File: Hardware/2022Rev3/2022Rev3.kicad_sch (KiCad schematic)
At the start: 101 parts, among them J1 Conn_01x04, J4 Conn_01x09, J5 Conn_01x09, J6 Conn_01x03, Q1 Q_NMOS_DGS, Q2 Q_NMOS_DGS, Q3 Q_NMOS_DSG, SW1 SW_SPDT, U1 ACS758xCB-200B-PFF, U2 LT1910, U3 TRS12433, U4 TRS12450, U5 Teensy4.1_DEV-16771, U6 Opamp_Dual, U7 Opamp_Dual, U8 Opamp_Dual, U9 Opamp_Dual

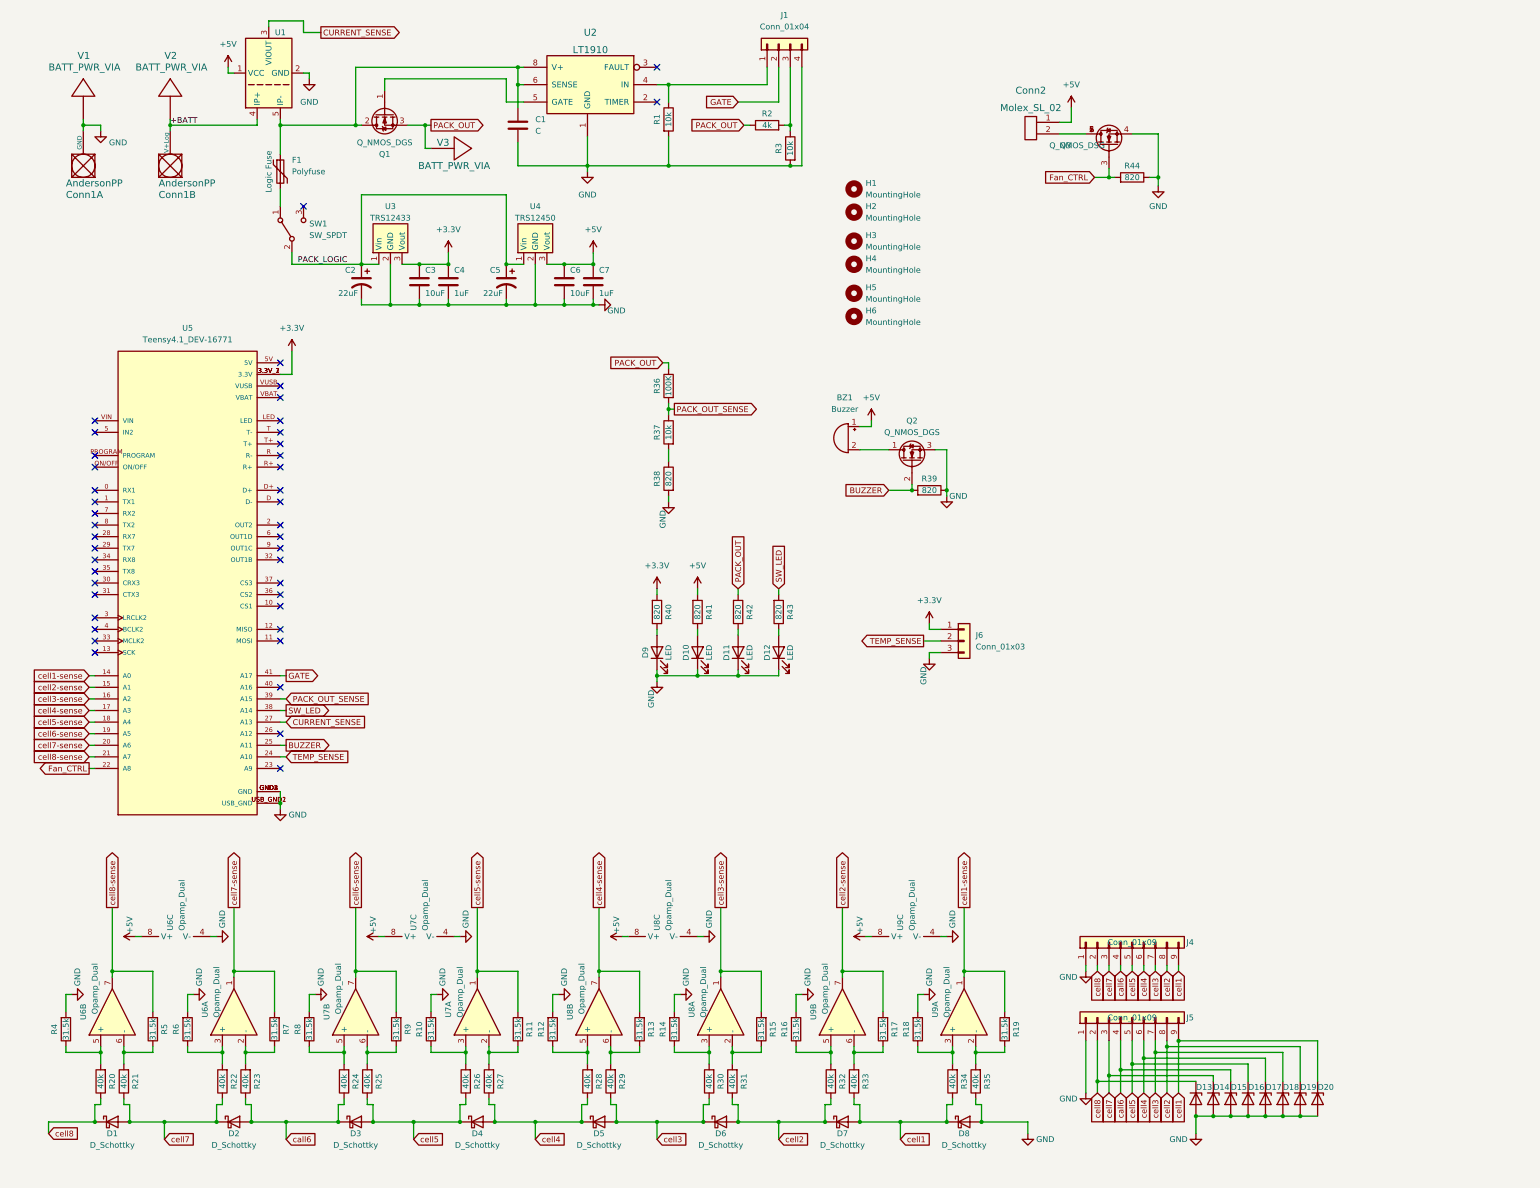
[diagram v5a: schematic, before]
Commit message: fixed led circuits
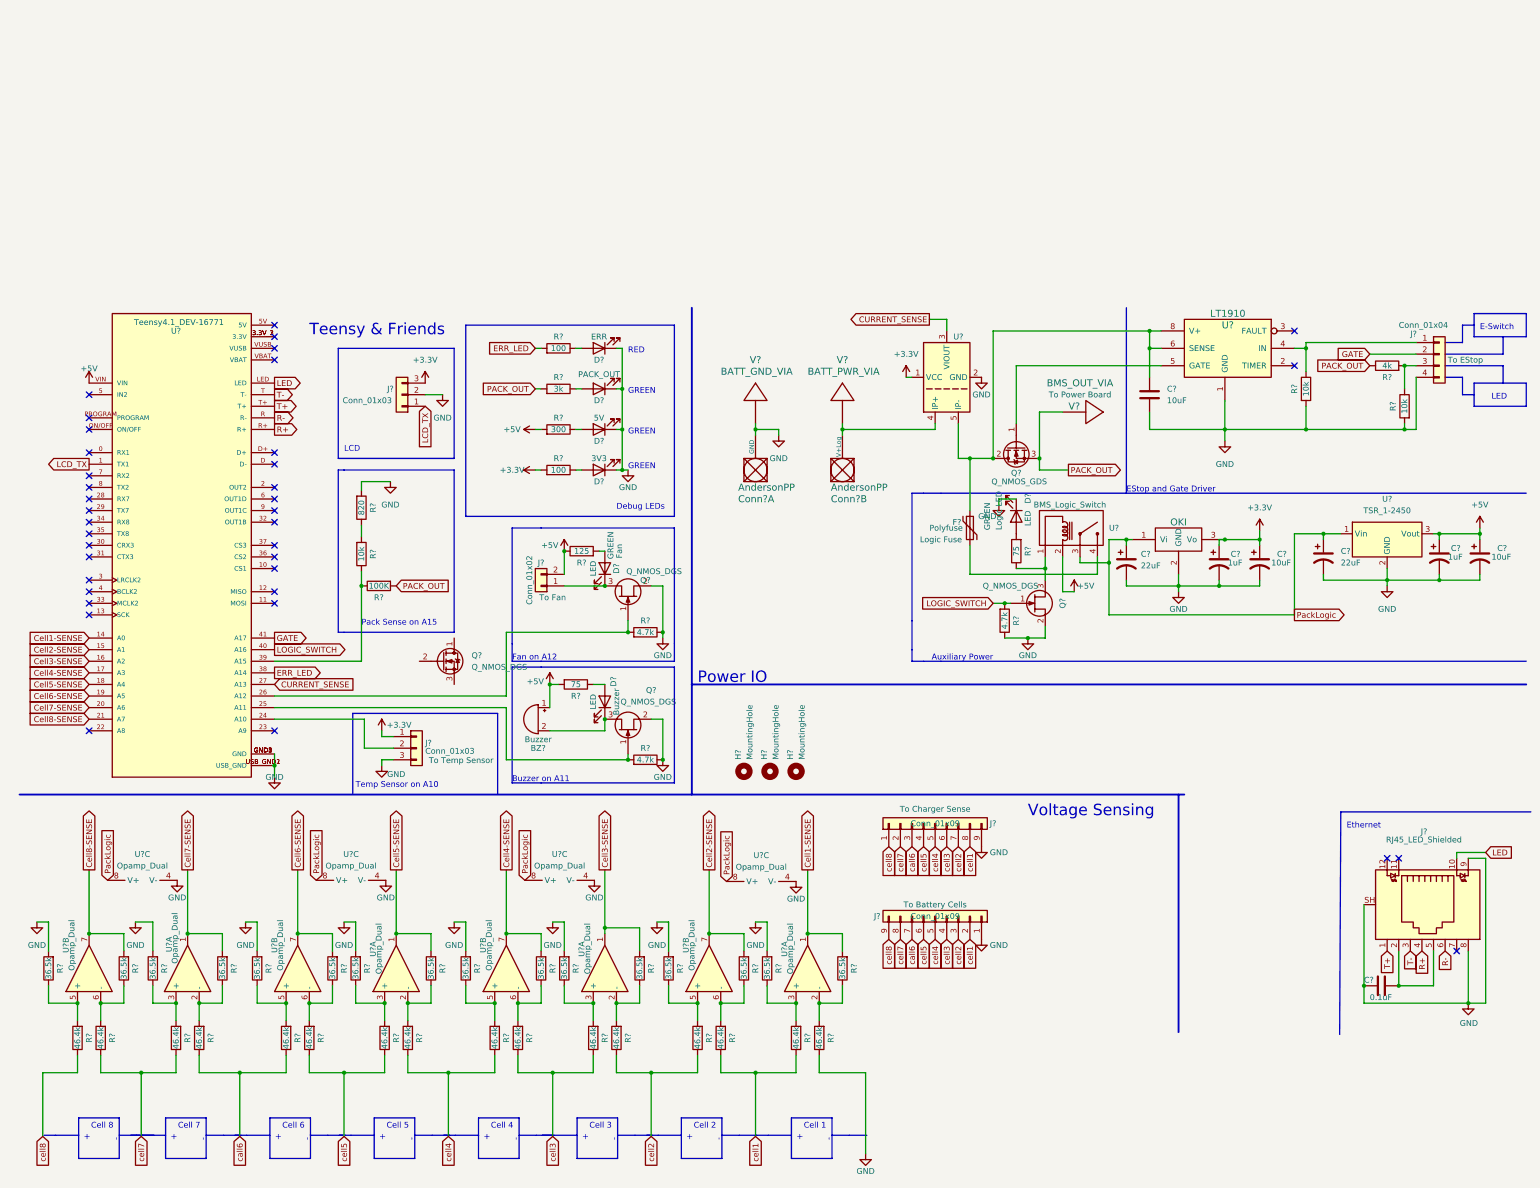
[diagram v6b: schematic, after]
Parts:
- removed BZ1: Buzzer, MRDT_Devices:BUZZER_SMI_1324_TW_5V_2_R, symbol Device:Buzzer
- removed C1: C, Capacitor_SMD:C_0603_1608Metric_Pad1.08x0.95mm_HandSolder, symbol Device:C
- removed C2, C5: 22uF, Capacitor_THT:CP_Radial_D5.0mm_P2.50mm, symbol Device:C_Polarized_US
- removed C3, C6: 10uF, Capacitor_SMD:C_0603_1608Metric_Pad1.08x0.95mm_HandSolder, symbol Device:C
- removed C4, C7: 1uF, Capacitor_SMD:C_0603_1608Metric_Pad1.08x0.95mm_HandSolder, symbol Device:C
- removed Conn1: AndersonPP, MRDT_Connectors:Square_Anderson_2_V_Side_By_Side_PV, symbol MRDT_Connectors:AndersonPP
- removed Conn2: Molex_SL_02, MRDT_Connectors:MOLEX_SL_02_Vertical, symbol MRDT_Connectors:Molex_SL_02
- removed D1, D2, D3, D4, D5, D6, D7, D8: D_Schottky, Diode_SMD:D_0603_1608Metric_Pad1.05x0.95mm_HandSolder, symbol Device:D_Schottky
- removed D10, D11, D12, D9: LED, LED_SMD:LED_0603_1608Metric_Pad1.05x0.95mm_HandSolder, symbol Device:LED
- removed D13, D14, D15, D16, D17, D18, D19, D20: D_Zener, Diode_SMD:D_0603_1608Metric_Pad1.05x0.95mm_HandSolder, symbol Device:D_Zener
- removed F1: Polyfuse, Fuse:Fuse_2920_7451Metric_Pad2.10x5.45mm_HandSolder, symbol Device:Polyfuse
- removed H1, H2, H3, H4: MountingHole, MRDT_Drill_Holes:4_40_Hole_Corner, symbol Mechanical:MountingHole
- removed H5, H6: MountingHole, MRDT_Drill_Holes:4_40_Hole, symbol Mechanical:MountingHole
- removed J1: Conn_01x04, MRDT_Connectors:MOLEX_SL_04_Vertical, symbol Connector_Generic:Conn_01x04
- removed J4, J5: Conn_01x09, MRDT_Connectors:MOLEX_SL_09_Vertical, symbol Connector_Generic:Conn_01x09
- removed J6: Conn_01x03, MRDT_Connectors:MOLEX_SL_03_Vertical, symbol Connector_Generic:Conn_01x03
- removed Q1: Q_NMOS_DGS, MRDT_Actives:IRLS3034_TO-263-7_P, symbol Device:Q_NMOS_GDS
- removed Q2: Q_NMOS_DGS, Package_TO_SOT_SMD:SOT-23_Handsoldering, symbol Device:Q_NMOS_DGS
- removed Q3: Q_NMOS_DSG, Package_TO_SOT_SMD:SuperSOT-6, symbol Device:Q_NMOS_DSG
- removed R1, R3, R37: 10k, Resistor_SMD:R_0603_1608Metric_Pad0.98x0.95mm_HandSolder, symbol Device:R
- removed R10, R11, R12, R13, R14, R15, R16, R17, R18, R19, R4, R5, R6, R7, R8, R9: 31.5k, Resistor_SMD:R_0603_1608Metric_Pad0.98x0.95mm_HandSolder, symbol Device:R
- removed R2: 4k, Resistor_SMD:R_0603_1608Metric_Pad0.98x0.95mm_HandSolder, symbol Device:R
- removed R20, R21, R22, R23, R24, R25, R26, R27, R28, R29, R30, R31, R32, R33, R34, R35: 40k, Resistor_SMD:R_0603_1608Metric_Pad0.98x0.95mm_HandSolder, symbol Device:R
- removed R36: 100K, Resistor_SMD:R_0603_1608Metric_Pad0.98x0.95mm_HandSolder, symbol Device:R
- removed R38, R39, R40, R41, R42, R43, R44: 820, Resistor_SMD:R_0603_1608Metric_Pad0.98x0.95mm_HandSolder, symbol Device:R
- removed SW1: SW_SPDT, MRDT_Connectors:MOLEX_SL_03_Vertical, symbol Switch:SW_SPDT
- removed U1: ACS758xCB-200B-PFF, Sensor_Current:Allegro_CB_PFF, symbol Sensor_Current:ACS758xCB-200B-PFF
- removed U2: LT1910, Package_SO:SO-8_3.9x4.9mm_P1.27mm, symbol MRDT_ICs:LT1910
- removed U3: TRS12433, MRDT_Devices:TSR_1-2433, symbol BMSRev3:TRS12433
- removed U4: TRS12450, MRDT_Devices:TSR_1-2433, symbol BMSRev3:TRS12433
- removed U5: Teensy4.1_DEV-16771, MRDT_Shields:MODULE_DEV-16771, symbol MRDT_Shields:Teensy4.1_DEV-16771
- removed U6, U7, U8, U9: Opamp_Dual, Package_SO:SO-8_3.9x4.9mm_P1.27mm, symbol Device:Opamp_Dual
- removed V1, V2, V3: BATT_PWR_VIA, MRDT_Drill_Holes:BATT_PWR_VIA, symbol MRDT_Drill_Holes:BATT_PWR_VIA
- added BZ?: Buzzer, MRDT_Devices:BUZZER_SMI_1324_TW_5V_2_R, symbol Device:Buzzer
- added C? (x2): 22uF, Capacitor_THT:CP_Radial_D5.0mm_P2.00mm, symbol Device:C_Polarized_US
- added C?: 10uF, Capacitor_SMD:C_1210_3225Metric_Pad1.33x2.70mm_HandSolder, symbol Device:C
- added C? (x2): 1uF, Capacitor_SMD:C_0603_1608Metric_Pad1.08x0.95mm_HandSolder, symbol Device:C_Polarized_US
- added C? (x2): 10uF, Capacitor_SMD:C_0603_1608Metric_Pad1.08x0.95mm_HandSolder, symbol Device:C_Polarized_US
- added C?: 0.1uF, Capacitor_SMD:C_0603_1608Metric_Pad1.08x0.95mm_HandSolder, symbol Device:C
- added Conn? (x2): AndersonPP, MRDT_Connectors:Square_Anderson_2_V_Side_By_Side, symbol MRDT_Connectors:AndersonPP
- added D? (x3): LED, LED_SMD:LED_0603_1608Metric_Pad1.05x0.95mm_HandSolder, symbol Device:LED
- added D?: ERR, LED_SMD:LED_0603_1608Metric_Pad1.05x0.95mm_HandSolder, symbol Device:LED
- added D?: 5V, LED_SMD:LED_0603_1608Metric_Pad1.05x0.95mm_HandSolder, symbol Device:LED
- added D?: PACK_OUT, LED_SMD:LED_0603_1608Metric_Pad1.05x0.95mm_HandSolder, symbol Device:LED
- added D?: 3V3, LED_SMD:LED_0603_1608Metric_Pad1.05x0.95mm_HandSolder, symbol Device:LED
- added F?: Polyfuse, Fuse:Fuse_2920_7451Metric_Pad2.10x5.45mm_HandSolder, symbol Device:Polyfuse
- added H? (x3): MountingHole, MRDT_Drill_Holes:4_40_Hole, symbol Mechanical:MountingHole
- added J?: RJ45_LED_Shielded, MRDT_Connectors:RJ45_Teensy, symbol Connector:RJ45_LED_Shielded
- added J? (x2): Conn_01x03, MRDT_Connectors:MOLEX_SL_03_Vertical, symbol Connector_Generic:Conn_01x03
- added J?: Conn_01x02, MRDT_Connectors:MOLEX_SL_02_Vertical, symbol Connector_Generic:Conn_01x02
- added J? (x2): Conn_01x09, MRDT_Connectors:MOLEX_SL_09_Vertical, symbol Connector_Generic:Conn_01x09
- added J?: Conn_01x04, MRDT_Connectors:MOLEX_SL_04_Vertical, symbol Connector_Generic:Conn_01x04
- added Q?: Q_NMOS_DGS, symbol Device:Q_NMOS_DGS
- added Q? (x3): Q_NMOS_DGS, Package_TO_SOT_SMD:SOT-23_Handsoldering, symbol Device:Q_NJFET_GSD
- added Q?: Q_NMOS_GDS, MRDT_Actives:IRLS3034_TO-263-7_P, symbol Device:Q_NMOS_GDS
- added R? (x16): 46.4k, Resistor_SMD:R_0603_1608Metric_Pad0.98x0.95mm_HandSolder, symbol Device:R
- added R? (x16): 36.5k, Resistor_SMD:R_0603_1608Metric_Pad0.98x0.95mm_HandSolder, symbol Device:R
- added R? (x3): 10k, Resistor_SMD:R_0603_1608Metric_Pad0.98x0.95mm_HandSolder, symbol Device:R
- added R? (x2): 100, Resistor_SMD:R_0603_1608Metric_Pad0.98x0.95mm_HandSolder, symbol Device:R
- added R?: 100K, Resistor_SMD:R_0603_1608Metric_Pad0.98x0.95mm_HandSolder, symbol Device:R
- added R? (x2): 75, Resistor_SMD:R_0603_1608Metric_Pad0.98x0.95mm_HandSolder, symbol Device:R
- added R? (x3): 4.7k, Resistor_SMD:R_0603_1608Metric_Pad0.98x0.95mm_HandSolder, symbol Device:R
- added R?: 4k, Resistor_SMD:R_0603_1608Metric_Pad0.98x0.95mm_HandSolder, symbol Device:R
- added R?: 3k, Resistor_SMD:R_0603_1608Metric_Pad0.98x0.95mm_HandSolder, symbol Device:R
- added R?: 125, Resistor_SMD:R_0603_1608Metric_Pad0.98x0.95mm_HandSolder, symbol Device:R
- added R?: 300, Resistor_SMD:R_0603_1608Metric_Pad0.98x0.95mm_HandSolder, symbol Device:R
- added R?: 820, Resistor_SMD:R_0603_1608Metric_Pad0.98x0.95mm_HandSolder, symbol Device:R
- added U? (x12): Opamp_Dual, Package_SO:SO-8_3.9x4.9mm_P1.27mm, symbol Device:Opamp_Dual
- added U?: Teensy4.1_DEV-16771, MRDT_Shields:Teensy_4_1_Ethernet, symbol MRDT_Shields:Teensy4.1_DEV-16771
- added U?: BMS_Logic_Switch, MRDT_Connectors:MOLEX_SL_04_Vertical, symbol MRDT_Switches:Relay_SPST
- added U?: LT1910, Package_SO:SO-8_3.9x4.9mm_P1.27mm, symbol MRDT_ICs:LT1910
- added U?: OKI, MRDT_Devices:OKI_Horizontal, symbol MRDT_Devices:OKI
- added U?: ACS758xCB-200B-PFF, Sensor_Current:Allegro_CB_PFF, symbol Sensor_Current:ACS758xCB-200B-PFF
- added U?: TSR_1-2450, Converter_DCDC:Converter_DCDC_TRACO_TSR-1_THT, symbol Regulator_Switching:TSR_1-2433
- added V?: BATT_GND_VIA, MRDT_Drill_Holes:BATT_PWR_VIA, symbol MRDT_Drill_Holes:BATT_PWR_VIA
- added V?: BMS_OUT_VIA, MRDT_Drill_Holes:BATT_PWR_VIA, symbol MRDT_Drill_Holes:BATT_PWR_VIA
- added V?: BATT_PWR_VIA, MRDT_Drill_Holes:BATT_PWR_VIA, symbol MRDT_Drill_Holes:BATT_PWR_VIA
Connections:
- net +5V: now also BZ?.1 (-), C?.1, C?.1, J?.2 (Pin_2), R?.1, R?.2, R?.2, U?.2, U?.3 (Vout), U?.VIN
- net CURRENT_SENSE: now also U?.27 (A13), U?.3 (VIOUT)
- net GATE: now also J?.2 (Pin_2), U?.41 (A17)
- net GND: now also C?.2, C?.2, C?.2, C?.2, C?.2, C?.2, C?.2, C?.2, Conn?.1 (GND), D?.1 (K), D?.1 (K), D?.1 (K), D?.1 (K), D?.1 (K), J?.1 (Pin_1), J?.2 (Pin_2), J?.3 (Pin_3), J?.4 (Pin_4), J?.8, J?.9, J?.9 (Pin_9), J?.SH, Q?.2 (S), Q?.2 (S), Q?.2 (S), R?.1, R?.1, R?.1, R?.1, R?.2, R?.2, R?.2, R?.2, R?.2, R?.2, R?.2, R?.2, R?.2, R?.2, R?.2, U?.1 (GND), U?.2 (GND), U?.2 (GND), U?.2 (GND), U?.4 (V-), U?.4 (V-), U?.4 (V-), U?.4 (V-), U?.GND1 (GND), U?.GND2 (GND), U?.GND3 (GND), U?.GND4 (GND), U?.GND5 (GND), U?.USB_GND1 (USB_GND), U?.USB_GND2 (USB_GND), V?.1
- net PACK_OUT: now also Q?.3 (S), R?.1, R?.2, R?.2, V?.1
- net call6: now also J?.3 (Pin_3), J?.7 (Pin_7), R?.1, R?.1
- net cell1: now also J?.2 (Pin_2), J?.8 (Pin_8), R?.1, R?.1
- net cell2: now also J?.3 (Pin_3), J?.7 (Pin_7), R?.1, R?.1
- net cell3: now also J?.4 (Pin_4), J?.6 (Pin_6), R?.1, R?.1
- net cell4: now also J?.5 (Pin_5), J?.5 (Pin_5), R?.1, R?.1
- net cell5: now also J?.4 (Pin_4), J?.6 (Pin_6), R?.1, R?.1
- net cell7: now also J?.2 (Pin_2), J?.8 (Pin_8), R?.1, R?.1
- net cell8: now also J?.1 (Pin_1), J?.9 (Pin_9), R?.1
- new net: D?.2 (A), R?.2 (x2)
- new net: R?.1, R?.2, U?.2 (-) (x4)
- new net: R?.1, R?.2, U?.3 (+) (x4)
- new net: J?.2 (Pin_2), U?.24 (A10)
- new net: Q?.1 (G), R?.2, U?.25 (A11)
- new net: Q?.1 (G), R?.2, U?.26 (A12)
- new net: U?.3.3V_1 (3.3V), U?.3.3V_2 (3.3V), U?.3.3V_3 (3.3V)
- new net: R?.1, R?.1, U?.39 (A15)
- new net: BZ?.2 (+), D?.1 (K), Q?.3 (D)
- new net: C?.1, J?.2, J?.5
- new net: R?.1, R?.2, U?.5 (+) (x4)
- new net: J?.1 (Pin_1), R?.1, U?.4 (IN)
- new net: D?.2 (A), R?.1 (x5)
- new net: Q?.3 (D), R?.1, U?.1
- new net: F?.2, U?.4
- new net: Q?.1 (G), U?.5 (GATE)
- new net: C?.1, F?.1, Q?.2 (D), U?.5 (IP-), U?.6 (SENSE), U?.8 (V+)
- new net: R?.1, R?.2, U?.6 (-) (x4)
- new net: R?.1, R?.2
- new net: D?.1 (K), J?.1 (Pin_1), Q?.3 (D)
- new net: Conn?.2 (V+Log), U?.4 (IP+), V?.1
- new net: J?.3 (Pin_3), R?.1, R?.2
- new net +3.3V: C?.1, C?.1, J?.1 (Pin_1), J?.3 (Pin_3), R?.2, U?.1 (VCC), U?.3 (Vo)
- new net Cell1-SENSE: R?.2, U?.1, U?.14 (A0)
- new net Cell2-SENSE: R?.2, U?.15 (A1), U?.7
- new net Cell3-SENSE: R?.2, U?.1, U?.16 (A2)
- new net Cell4-SENSE: R?.2, U?.17 (A3), U?.7
- new net Cell5-SENSE: R?.2, U?.1, U?.18 (A4)
- new net Cell6-SENSE: R?.2, U?.19 (A5), U?.7
- new net Cell7-SENSE: R?.2, U?.1, U?.20 (A6)
- new net Cell8-SENSE: R?.2, U?.21 (A7), U?.7
- new net ERR_LED: R?.2, U?.38 (A14)
- new net LCD_TX: J?.1 (Pin_1), U?.1 (TX1)
- new net LED: J?.10, U?.LED
- new net LOGIC_SWITCH: Q?.1 (G), R?.2, U?.40 (A16)
- new net PackLogic: C?.1, C?.1, U?.1 (Vi), U?.1 (Vin), U?.3, U?.8 (V+), U?.8 (V+), U?.8 (V+), U?.8 (V+)
- new net R+: J?.4, U?.R+
- new net R-: J?.6, U?.R (R-)
- new net T+: J?.1, U?.T+
- new net T-: J?.3, U?.T (T-)
- no-connect marks 43 -> 38
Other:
- note added: "+"
- note added: "-"
- note added: "Auxiliary Power"
- note added: "Buzzer on A11"
- note added: "Cell 1"
- note added: "Cell 2"
- note added: "Cell 3"
- note added: "Cell 4"
- note added: "Cell 5"
- note added: "Cell 6"
- note added: "Cell 7"
- note added: "Cell 8"
- note added: "Debug LEDs"
- note added: "E-Switch"
- note added: "EStop and Gate Driver"
- note added: "Ethernet"
- note added: "Fan on A12"
- note added: "GREEN"
- note added: "LCD"
- note added: "LED"
- note added: "Pack Sense on A15"
- note added: "Power IO"
- note added: "RED"
- note added: "Teensy & Friends"
- note added: "Temp Sensor on A10"
- note added: "Voltage Sensing"

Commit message: Schematic organized and updated with everything except cell balancing
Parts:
- removed Q? (x3): Q_NMOS_DGS, Package_TO_SOT_SMD:SOT-23_Handsoldering, symbol Device:Q_NJFET_GSD
- added Q? (x2): Q_NMOS_DGS, symbol Device:Q_NMOS_DGS
- R?: value 75 -> 120
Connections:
- net +5V: now also R?.2
- net GND: now also Q?.3 (S), Q?.3 (S), Q?.3 (S); no longer D?.1 (K)
- net LOGIC_SWITCH: now also Q?.2 (G)
- net PackLogic: now also U?.4; no longer U?.3
- net at D?.2 (A): now also R?.1; no longer R?.2
- net at Q?.1 (D): now also BZ?.2 (+), D?.1 (K)
- net BUZZER_CTRL: now reaches Q?.2 (G)
- net BUZZER_CTRL: now also R?.2, U?.25 (A11)
- net TEMP_SENSE: now reaches J?.2 (Pin_2), U?.24 (A10)
- net FAN_CTRL: now reaches R?.2, U?.26 (A12)
- net FAN_CTRL: now also Q?.2 (G)
- net PACK_SENSE: now reaches R?.1, R?.1, U?.39 (A15)
- net at U?.1: now also D?.1 (K), Q?.1 (D); no longer R?.1
- net at F?.2: now also U?.3; no longer U?.4
- net at D?.1 (K), J?.1 (Pin_1): now also Q?.1 (D)
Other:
- note removed: "Teensy & Friends"
- note removed: "Voltage Sensing"
- moved on the sheet: BZ?, C?, Conn?A, Conn?B, D?, F?, H?, J?, Q?, R?, U?, U?A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
